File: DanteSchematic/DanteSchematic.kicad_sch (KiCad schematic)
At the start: 1 part

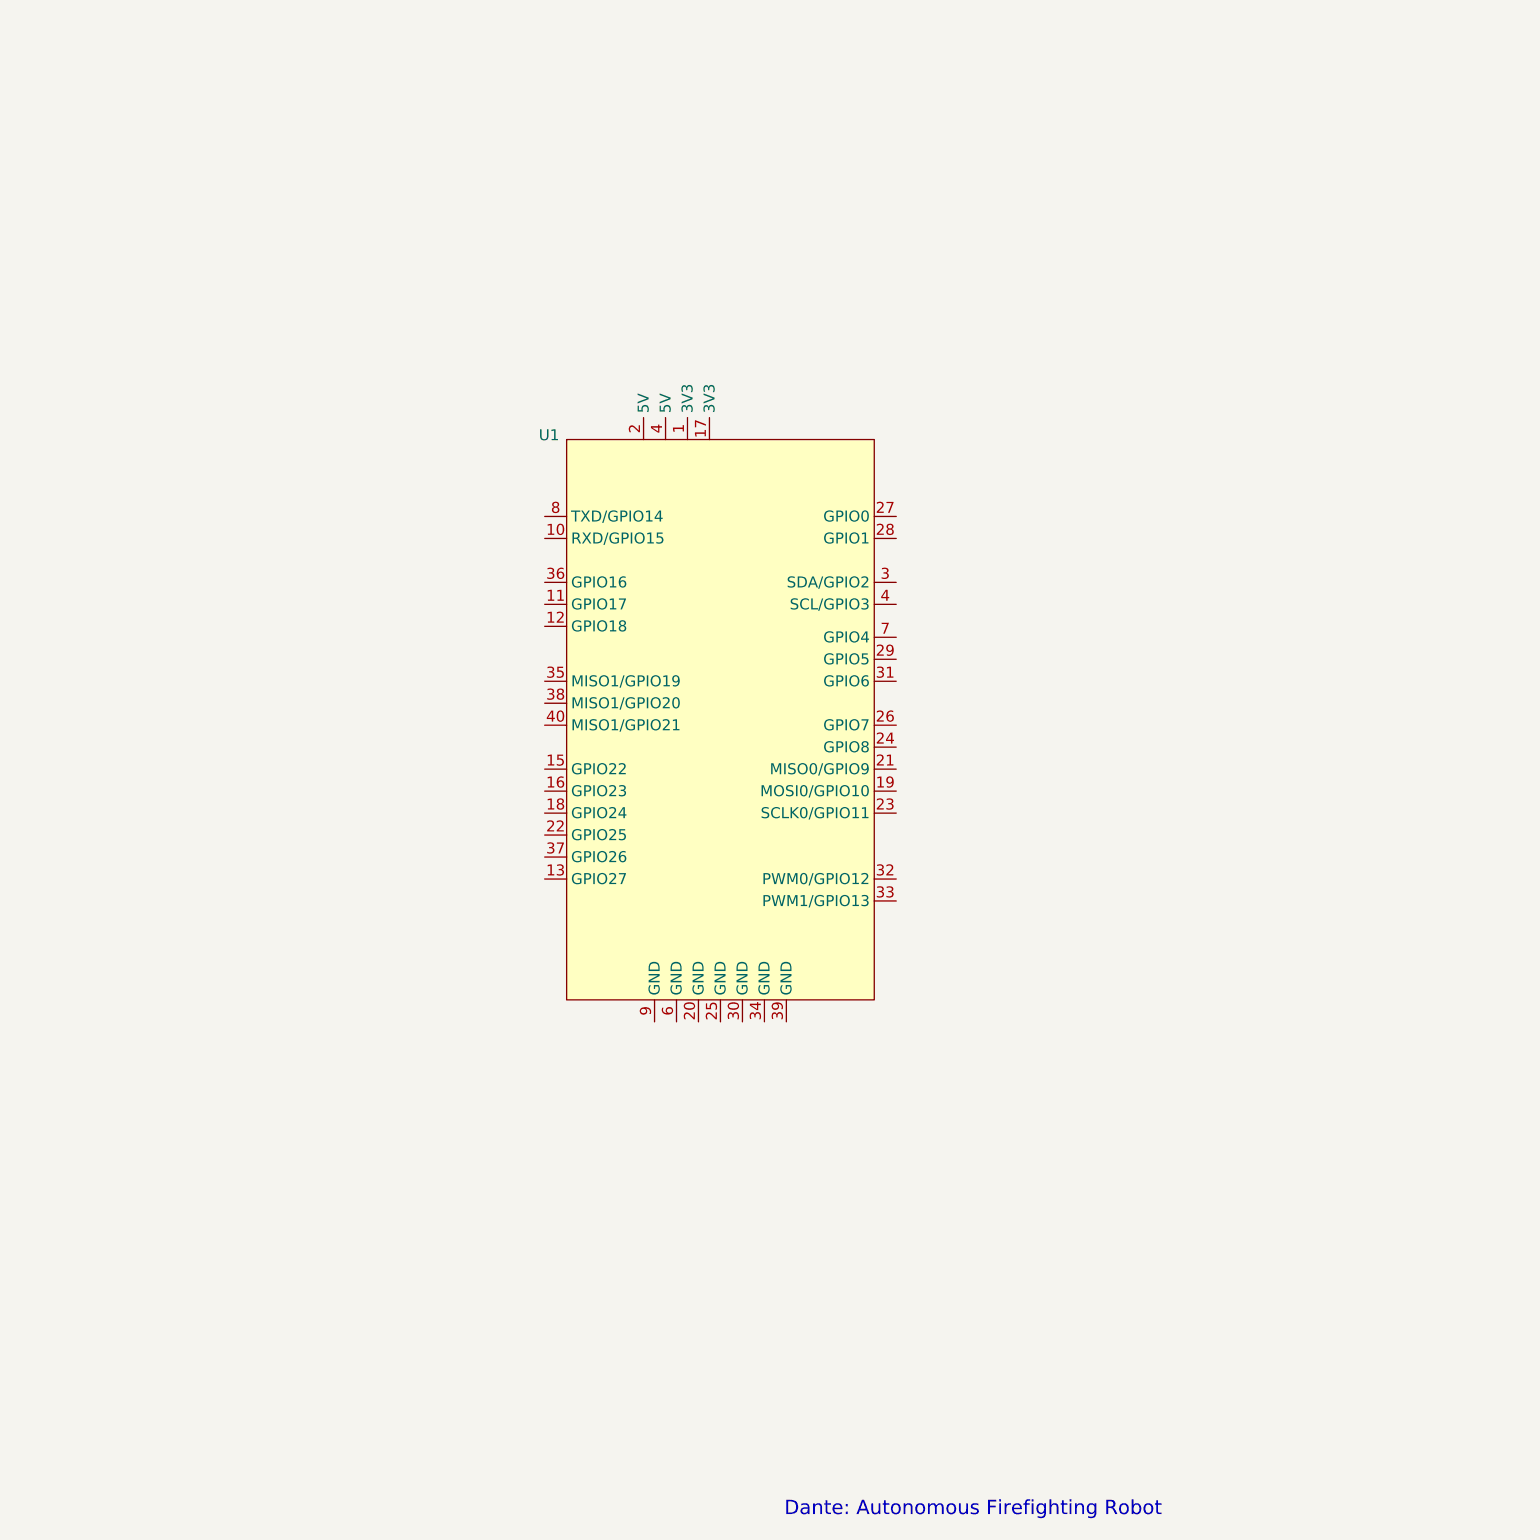
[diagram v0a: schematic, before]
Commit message: Added KiCad file for car schematic
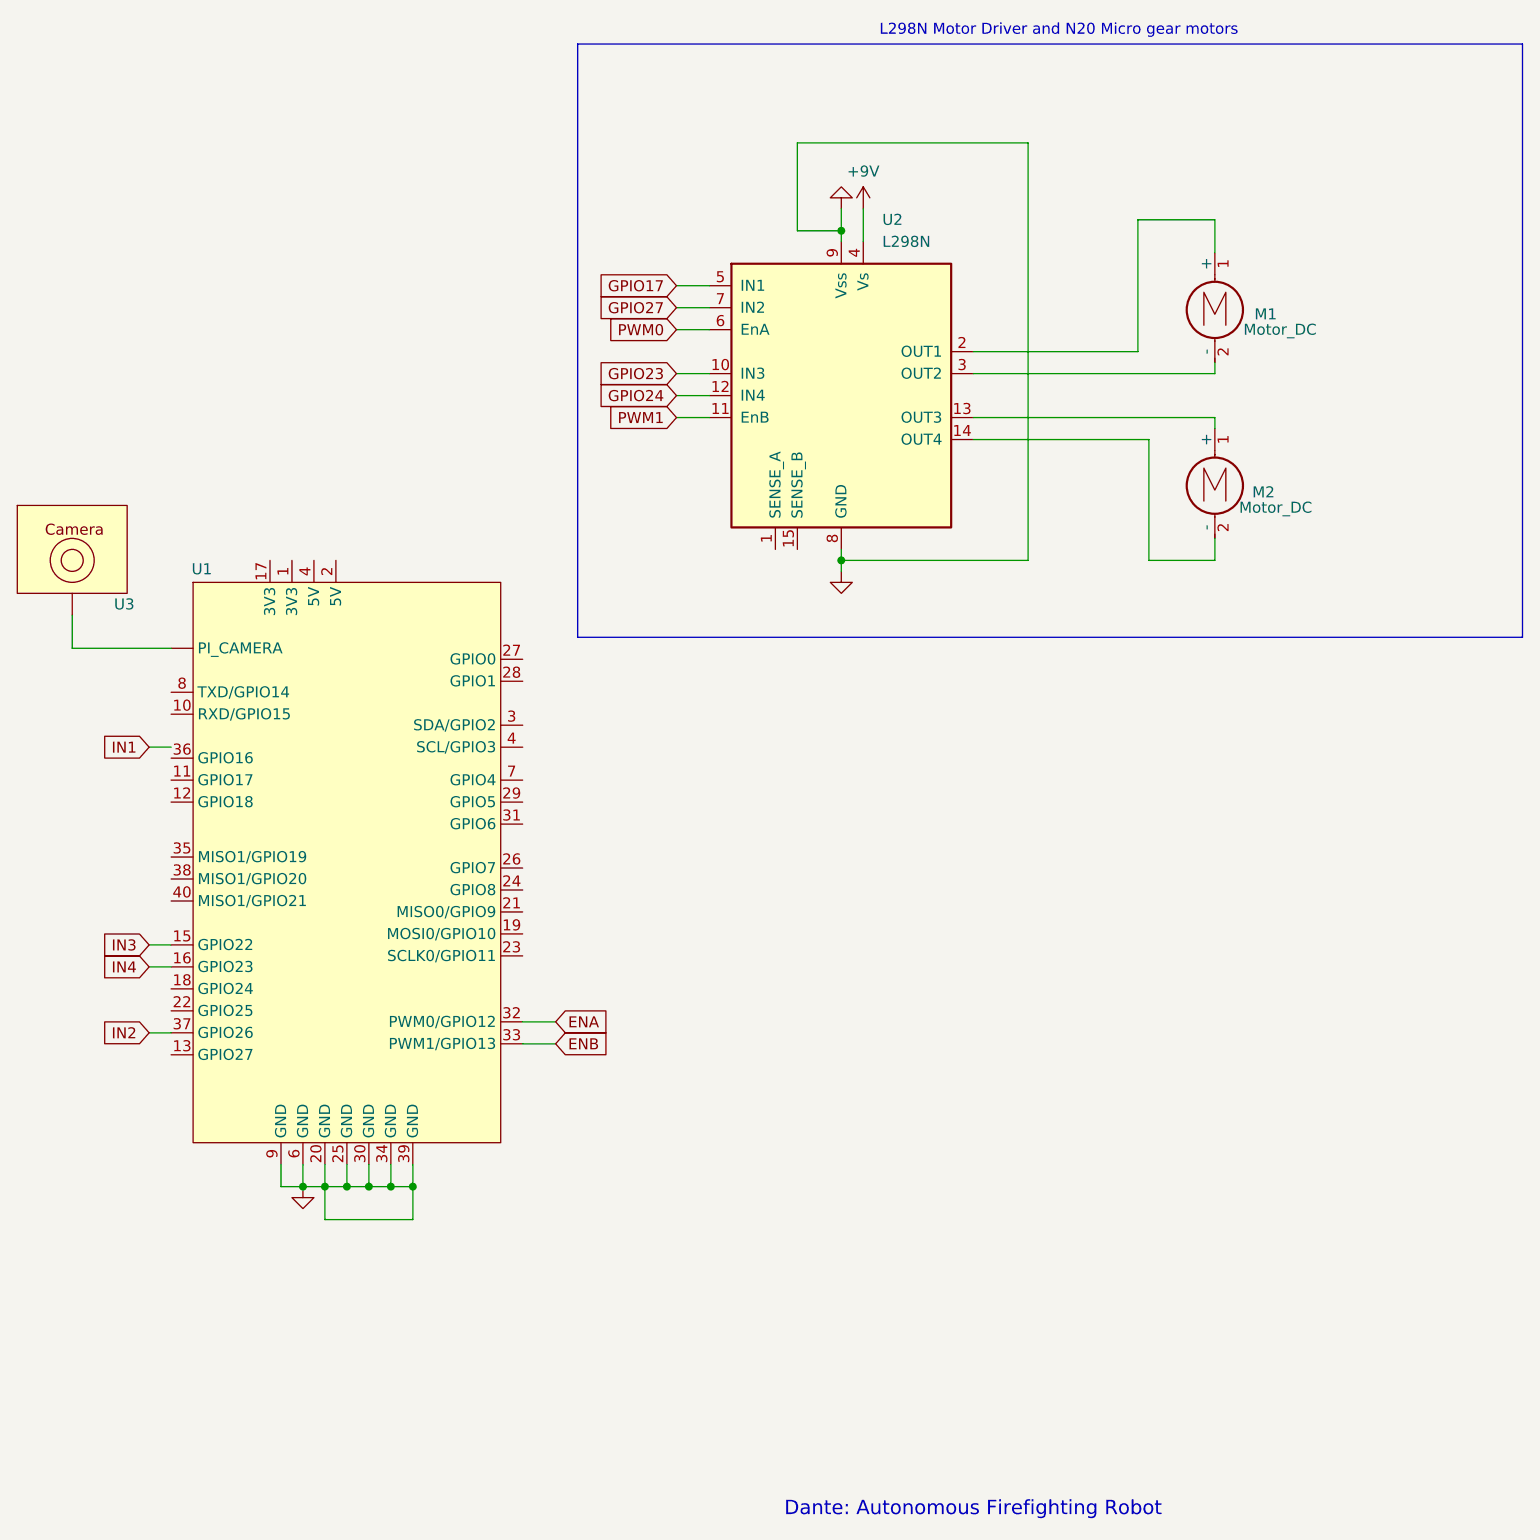
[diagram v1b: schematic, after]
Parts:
- added M1, M2: Motor_DC, symbol Motor:Motor_DC
- added U2: L298N, Package_TO_SOT_THT:TO-220-15_P2.54x2.54mm_StaggerOdd_Lead4.58mm_Vertical, symbol Driver_Motor:L298N
- added U3: ~, symbol CarSchematics:Raspberry_Pi_Camera_V3
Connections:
- net IN3: now reaches U1.15 (GPIO22)
- net IN4: now reaches U1.16 (GPIO23)
- net GND: now reaches U1.20 (GND)
- net GND: now also U1.25 (GND), U1.30 (GND), U1.34 (GND), U1.39 (GND), U1.6 (GND), U1.9 (GND), U2.8 (GND), U2.9 (Vss)
- net ENA: now reaches U1.32 (PWM0/GPIO12)
- net ENB: now reaches U1.33 (PWM1/GPIO13)
- net IN2: now reaches U1.37 (GPIO26)
- new net: M2.1 (+), U2.13 (OUT3)
- new net: M2.2 (-), U2.14 (OUT4)
- new net: M1.1 (+), U2.2 (OUT1)
- new net: M1.2 (-), U2.3 (OUT2)
- new net: U1. (PI_CAMERA), U3.
- new net +9V: U2.4 (Vs)
- new net GPIO17: U2.5 (IN1)
- new net GPIO23: U2.10 (IN3)
- new net GPIO24: U2.12 (IN4)
- new net GPIO27: U2.7 (IN2)
- new net PWM0: U2.6 (EnA)
- new net PWM1: U2.11 (EnB)
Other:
- note added: "L298N Motor Driver and N20 Micro gear motors"
